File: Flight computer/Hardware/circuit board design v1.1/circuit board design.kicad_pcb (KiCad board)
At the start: 4 copper layers, 30.5 x 82.6 mm, 89 parts, among them J1 Conn_01x05, J2 USB_B_Micro, J3 Screw_Terminal_01x04, J4 Conn_01x02, J5 Screw_Terminal_01x04, J6 Conn_Coaxial, J7 Conn_Coaxial, U1 IIS2MDC, U10 BMI088, U11 W25Q64JVSSIM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

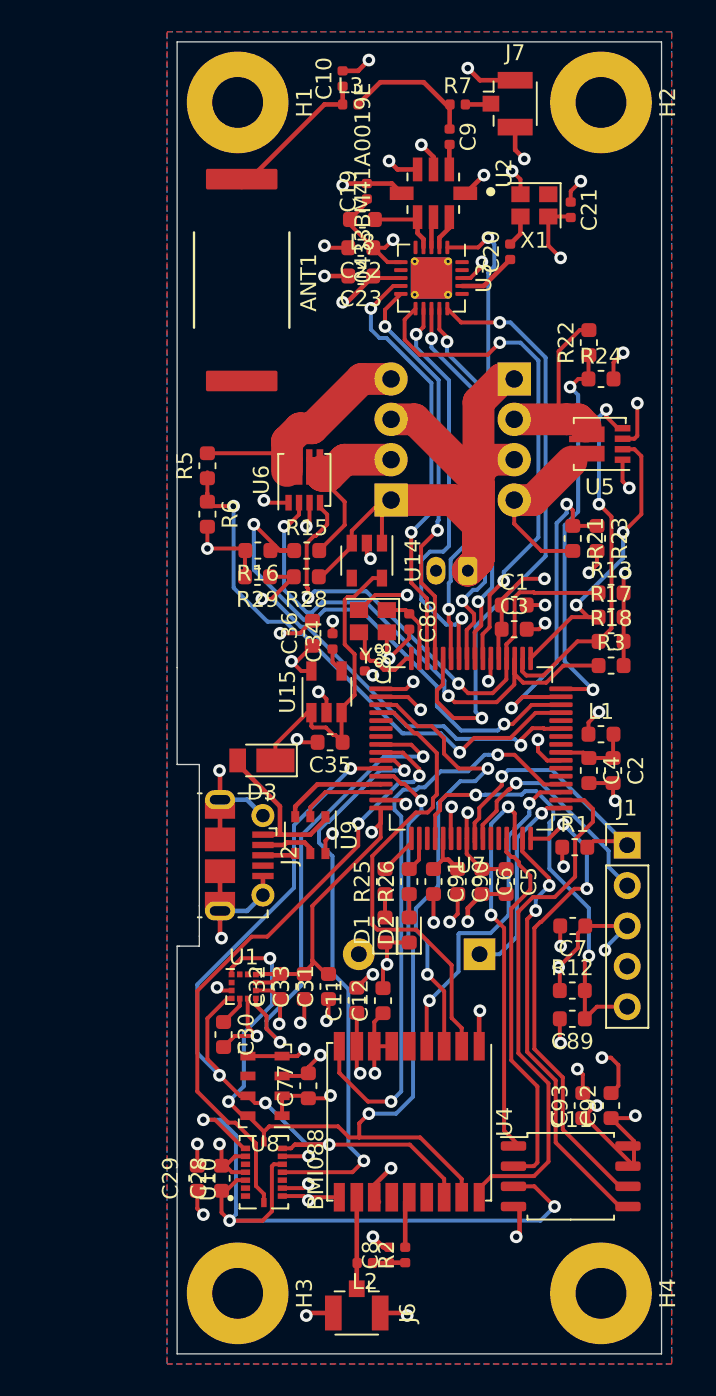
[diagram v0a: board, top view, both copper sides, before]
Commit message: wired up the news sensors
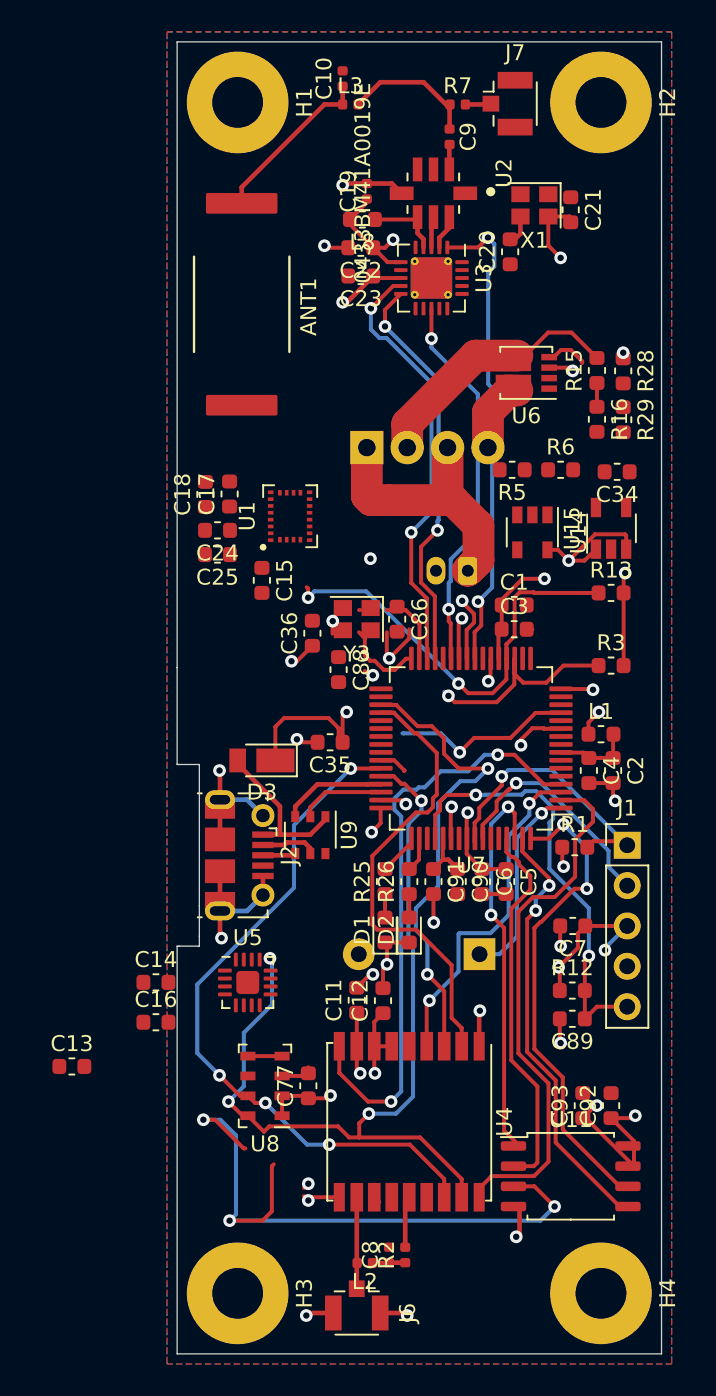
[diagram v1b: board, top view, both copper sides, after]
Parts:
- removed C28, C29, C31, C33: 100nF, Capacitor_SMD:C_0603_1608Metric
- removed C30: 220nF, Capacitor_SMD:C_0603_1608Metric
- removed C32: 10uF, Capacitor_SMD:C_0603_1608Metric
- removed J5: Screw_Terminal_01x04, flight-computer:TerminalBlock_TE_282834-4_1x04_P2.54mm_Horizontal
- removed R17, R18: 3.3K, Resistor_SMD:R_0603_1608Metric
- removed R21, R22: 100K, Resistor_SMD:R_0603_1608Metric
- removed R23, R24: 27K, Resistor_SMD:R_0603_1608Metric
- removed U10: BMI088, BMI088:PQFN50P450X300X100-16N
- added C13: 10uF, Capacitor_SMD:C_0603_1608Metric, F.Cu at (85.7, 122.3)
- added C14: 100nF, Capacitor_SMD:C_0603_1608Metric, F.Cu at (91.0, 117.0)
- added C15: 100nF, Capacitor_SMD:C_0603_1608Metric, F.Cu at (97.7, 91.7)
- added C16: 100nF, Capacitor_SMD:C_0603_1608Metric, F.Cu at (91.0, 119.5)
- added C17: 100nF, Capacitor_SMD:C_0603_1608Metric, F.Cu at (95.6, 86.2)
- added C18: 10uF, Capacitor_SMD:C_0603_1608Metric, F.Cu at (94.1, 86.3)
- added C24: 10nF, Capacitor_SMD:C_0603_1608Metric, F.Cu at (94.9, 88.5)
- added C25: 100nF, Capacitor_SMD:C_0603_1608Metric, F.Cu at (94.9, 90.0)
- C20, C21, C34, C86, C88: footprint Capacitor_SMD:C_0402_1005Metric -> Capacitor_SMD:C_0603_1608Metric
- U1: value IIS2MDC -> LSM9DS1; footprint Package_LGA:LGA-12_2x2mm_P0.5mm -> Package_LGA:LGA-24L_3x3.5mm_P0.43mm
- U15: value LD3985G33R_TSOT23 -> LD3985M33R_TSOT23
- U5: value Si7232DN -> H3LIS100DL; footprint Package_SO:Vishay_PowerPAK_1212-8_Dual -> Package_DFN_QFN:QFN-16-1EP_3x3mm_P0.5mm_EP1.45x1.45mm
- X1: footprint Crystal:Crystal_SMD_2520-4Pin_2.5x2.0mm -> flight-computer:Crystal_SMD_2520-4Pin_2.5x2.0mm
- moved U5 40.5 mm to (96.8, 117.0), turned to 0 degrees
- moved U1 29.7 mm to (99.4, 87.6), turned to 90 degrees
- moved R29 25.0 mm to (120.4, 81.6), turned to 270 degrees
- moved R28 23.8 mm to (120.4, 78.5), turned to 270 degrees
- moved R16 22.9 mm to (118.7, 81.5), turned to 270 degrees
- moved R6 22.4 mm to (116.5, 84.7), turned to 0 degrees
- moved R15 21.5 mm to (118.7, 78.5), turned to 90 degrees
- moved C34 20.8 mm to (120.0, 84.8), turned to 180 degrees
- moved U15 20.7 mm to (119.6, 88.4)
- moved R5 19.2 mm to (113.4, 84.7), turned to 180 degrees
- moved U6 15.5 mm to (114.3, 78.6), turned to 180 degrees
- moved U14 10.6 mm to (114.7, 88.6)
- moved J3 3.64 mm to (104.3, 83.3), turned to 0 degrees
- moved C88 1.70 mm to (102.5, 97.3)
- moved ANT1 1.52 mm to (96.4, 74.3)
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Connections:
- U1 pad 1: /gps/GPS_SCL -> +3V3
- U1 pad 10: +3V3 -> Net-(U1-Pad10)
- U1 pad 11: Net-(U1-Pad11) -> /sensors/ACCL_RDY
- U1 pad 12: Net-(U1-Pad12) -> /sensors/GYRO_RDY
- U1 pad 2: Net-(U1-Pad2) -> /gps/GPS_SCL
- U1 pad 5: Net-(C30-Pad1) -> +3V3
- U1 pad 6: GND -> +3V3
- U1 pad 7: /sensors/MAG_RDY -> +3V3
- U1 pad 8: GND -> +3V3
- U1 pad 9: +3V3 -> /sensors/MAG_RDY
- U5 pad 1: GND -> +3V3
- U5 pad 2: /pyro_driver/FIRE_C -> (no net)
- U5 pad 3: GND -> (no net)
- U5 pad 4: /pyro_driver/FIRE_D -> /gps/GPS_SCL
- U5 pad 5: /pyro_driver/FET_D -> GND
- U5 pad 6: /pyro_driver/FET_C -> /gps/GPS_SDA
- U7 pad 15: /MCU/MCU_PA06 -> Net-(U7-Pad15)
- U7 pad 16: /MCU/MCU_PA07 -> Net-(U7-Pad16)
- U7 pad 17: /pyro_driver/FIRE_C -> Net-(U7-Pad17)
- U7 pad 18: /pyro_driver/FIRE_D -> Net-(U7-Pad18)
- U7 pad 37: Net-(U7-Pad37) -> /sensors/GYRO_RDY
- U7 pad 38: Net-(U7-Pad38) -> /sensors/ACCL_RDY
- U7 pad 41: /sensors/ACCL_RDY -> /sensors/H_ACCL_INT1
- U7 pad 42: /sensors/GYRO_RDY -> /sensors/H_ACCL_INT2
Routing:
- net GND: track 158.6 -> 72.4 mm, vias 64 -> 25
- net +3V3: track 278.7 -> 222.4 mm, vias 23 -> 20
- net /sensors/ACCL_RDY: track 39.0 -> 0.00 mm, vias 2 -> 0
- net /MCU/MCU_NSEL1: track 38.2 -> 0.00 mm, vias 2 -> 0
- net /sensors/GYRO_RDY: track 36.1 -> 0.00 mm, vias 2 -> 0
- net Vdrive: track 53.2 -> 19.4 mm, vias 0 -> 1
- net /MCU/MCU_PB10: track 32.0 -> 0.00 mm, vias 2 -> 0
- net /MCU/MCU_PA05: track 33.0 -> 2.39 mm, vias 2 -> 0
- net /sensors/MAG_RDY: track 30.4 -> 0.00 mm, vias 2 -> 0
- net /MCU/MCU_PA07: track 25.3 -> 0.00 mm, vias 2 -> 0
- net /MCU/MCU_PB08: track 27.4 -> 3.16 mm, vias 2 -> 1
- net /MCU/MCU_SCLK1: track 26.6 -> 2.63 mm, vias 2 -> 1
- net /pyro_driver/FIRE_D: track 23.8 -> 0.00 mm, vias 2 -> 0
- net /MCU/MCU_PA04: track 34.8 -> 11.5 mm, vias 2 -> 1
- net /MCU/MCU_PA06: track 20.7 -> 0.00 mm, vias 2 -> 0
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
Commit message: Fully routed board v1.1 with the new high g accelerometer
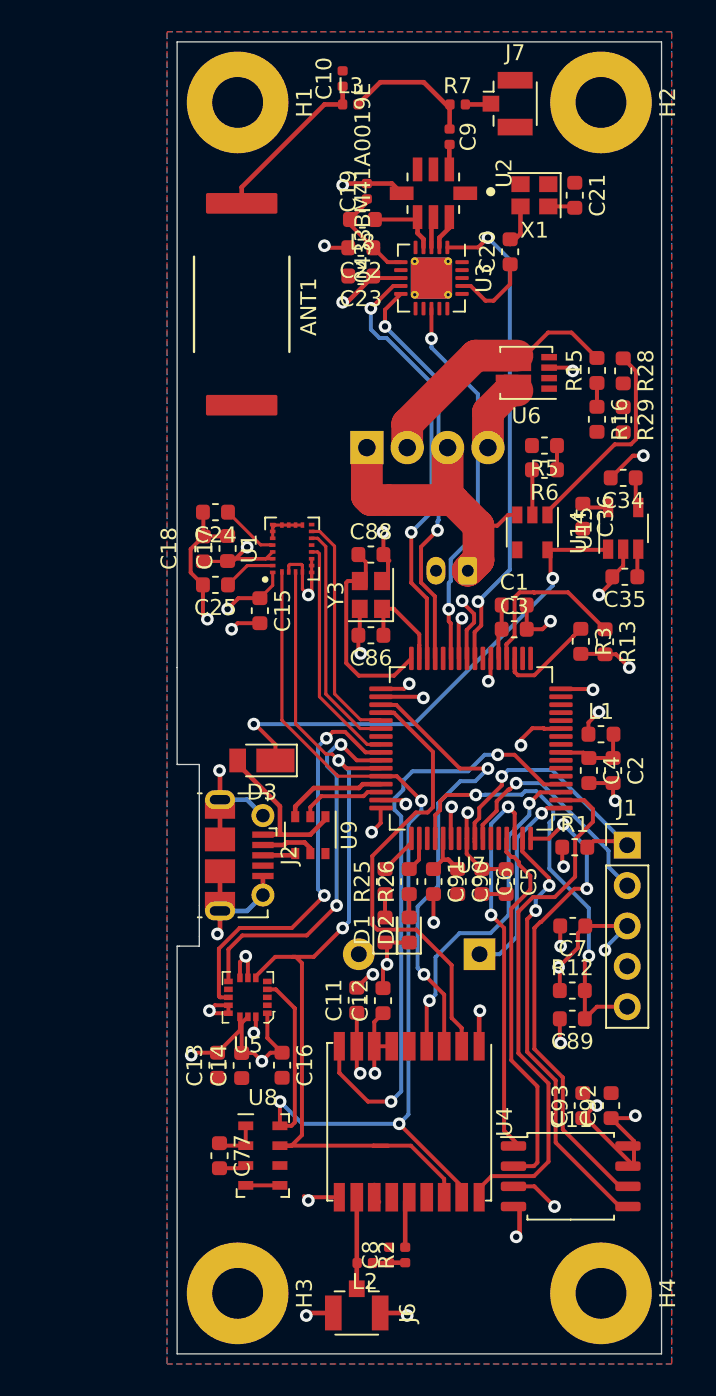
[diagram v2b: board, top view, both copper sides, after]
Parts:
- U5: footprint Package_DFN_QFN:QFN-16-1EP_3x3mm_P0.5mm_EP1.45x1.45mm -> flight-computer:TFLGA-16_3x3mm
- moved C35 21.3 mm to (120.5, 91.4)
- moved C36 18.5 mm to (117.9, 87.6), turned to 270 degrees
- moved C13 9.16 mm to (94.9, 122.2), turned to 90 degrees
- moved C16 8.38 mm to (98.9, 122.2), turned to 270 degrees
- moved C88 7.52 mm to (104.5, 90.0), turned to 0 degrees
- moved C14 7.52 mm to (96.4, 122.2), turned to 90 degrees
- moved C77 7.11 mm to (95.0, 127.9), turned to 270 degrees
- moved U8 4.39 mm to (97.7, 127.9), turned to 0 degrees
- moved C17 3.43 mm to (95.5, 89.7)
- moved C18 3.43 mm to (94.0, 89.7)
- moved R13 3.10 mm to (119.3, 95.5), turned to 270 degrees
- moved R5 2.54 mm to (115.4, 83.2)
- moved R3 2.44 mm to (117.7, 95.5), turned to 270 degrees
- moved U1 2.04 mm to (99.6, 89.7)
- moved C86 1.94 mm to (104.5, 95.1), turned to 180 degrees
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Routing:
- net +3V3: track 222.4 -> 171.5 mm, vias 20 -> 19
- net GND: track 72.4 -> 100.5 mm, vias 25 -> 30
- net /sensors/H_ACCL_INT1: track 0.00 -> 26.0 mm, vias 0 -> 2
- net /sensors/H_ACCL_INT2: track 1.77 -> 23.8 mm, vias 0 -> 2
- net /pyro_driver/FIRE_B: track 29.8 -> 10.9 mm, vias 2 -> 0
- net /gps/GPS_SDA: track 43.8 -> 60.4 mm, vias 4 -> 2
- net Vdrive: track 19.4 -> 35.2 mm, vias 1 -> 0
- net /sensors/ACCL_RDY: track 0.00 -> 14.8 mm
- net /sensors/GYRO_RDY: track 0.00 -> 14.7 mm
- net /sensors/MAG_RDY: track 0.00 -> 14.6 mm
- net /gps/GPS_SCL: track 56.0 -> 67.8 mm, vias 4 -> 3
- net /MCU/MCU_PA04: track 11.5 -> 1.52 mm, vias 1 -> 0
- net /pyro_driver/FIRE_A: track 13.7 -> 6.31 mm, vias 1 -> 0
- net /MCU/XOUT: track 5.19 -> 12.5 mm
- net Net-(C35-Pad1): track 39.8 -> 33.7 mm
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
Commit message: flood fill top and bottom layers
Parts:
- moved C15 2.68 mm to (97.3, 96.2)
- moved C18 2.68 mm to (93.7, 92.4)
- moved C24 2.68 mm to (94.5, 90.0)
- moved C25 2.68 mm to (94.5, 94.6)
- moved C17 2.68 mm to (95.2, 92.3)
- moved U1 2.68 mm to (99.3, 92.3)
- moved R13 1.66 mm to (117.6, 95.4)
- moved J4 1.52 mm to (110.6, 89.5)
- moved R3 1.40 mm to (119.1, 95.4)
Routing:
- net GND: track 100.5 -> 172.5 mm, vias 30 -> 53
- net /MCU/MCU_NSEL1: track 0.00 -> 37.6 mm, vias 0 -> 2
- net /MCU/MCU_PB10: track 0.00 -> 32.2 mm, vias 0 -> 2
- net /MCU/MCU_PB08: track 3.16 -> 30.9 mm, vias 1 -> 2
- net /MCU/MCU_SCLK1: track 2.63 -> 27.6 mm, vias 1 -> 2
- net /MCU/MCU_MOSI1: track 4.15 -> 28.4 mm, vias 1 -> 2
- net /MCU/MCU_PA04: track 1.52 -> 24.2 mm, vias 0 -> 2
- net /MCU/MCU_PA05: track 2.39 -> 24.9 mm, vias 0 -> 2
- net /pyro_driver/FIRE_A: track 6.31 -> 28.7 mm, vias 0 -> 2
- net /pyro_driver/FIRE_B: track 10.9 -> 29.5 mm, vias 0 -> 2
- net +3V3: track 171.5 -> 180.3 mm, vias 19 -> 25
- net /MCU/MCU_MISO1: track 24.0 -> 32.2 mm
- net /MCU/MCU_PA12: track 25.6 -> 33.6 mm, vias 2 -> 0
- net /MCU/MCU_PA13: track 27.3 -> 34.4 mm, vias 2 -> 0
- net /pyro_driver/FET_A: track 4.65 -> 9.31 mm
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- added copper zone on B.Cu, net (none)
- removed copper zone on B.Cu, net GND

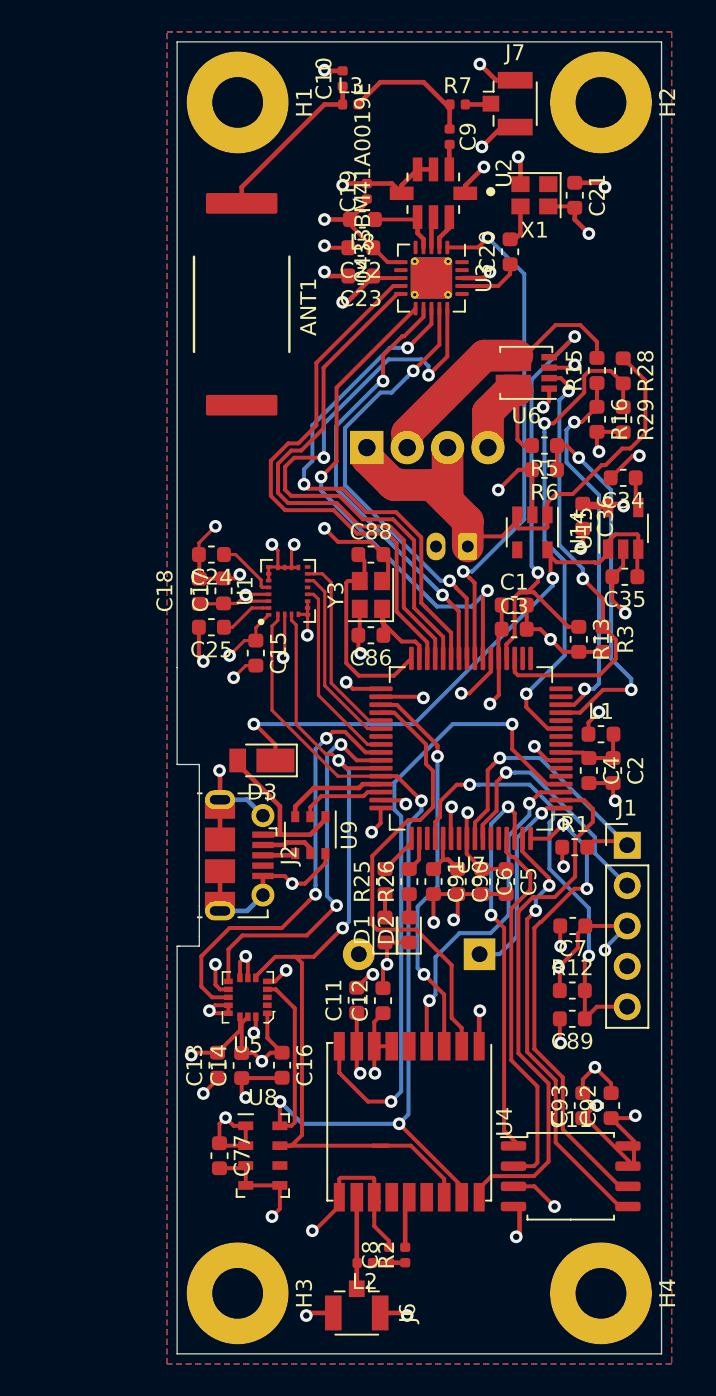
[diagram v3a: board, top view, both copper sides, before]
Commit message: put in logo for V1.1
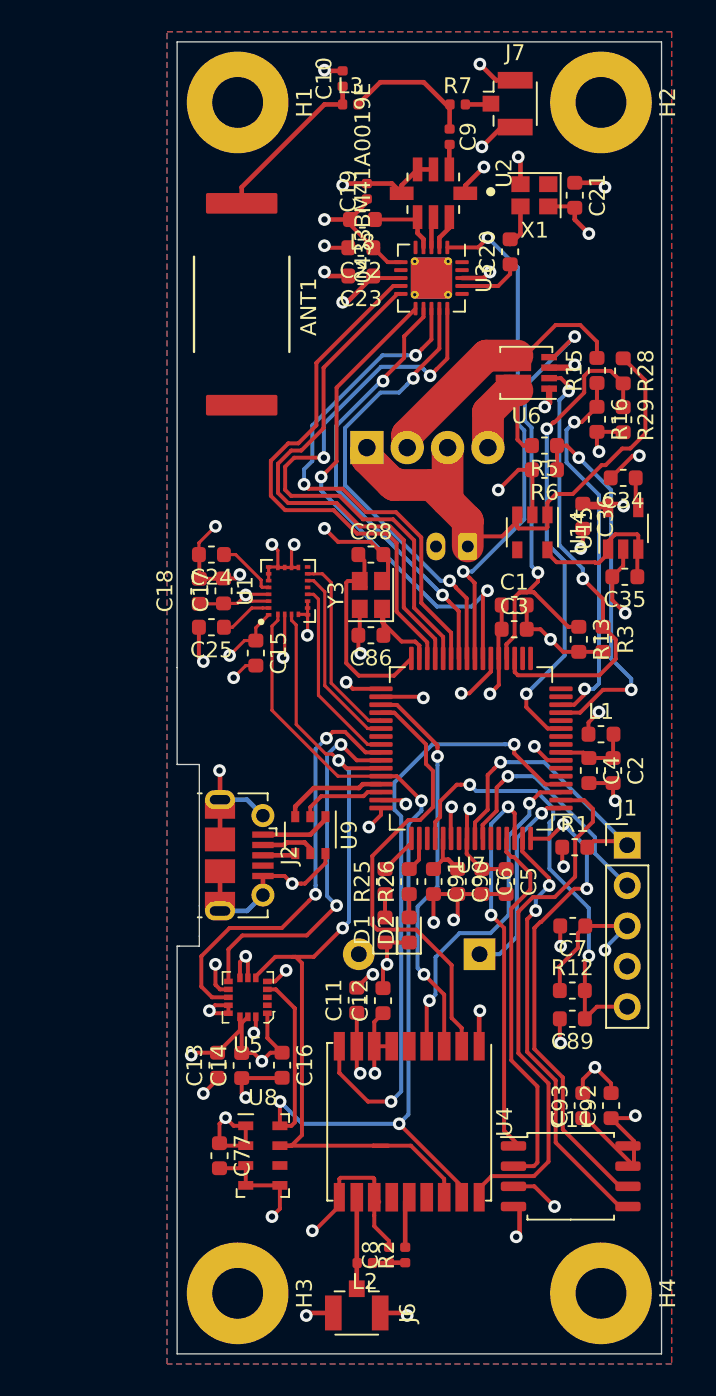
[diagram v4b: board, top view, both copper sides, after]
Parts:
- removed D3: DFLS130L, Diode_SMD:D_PowerDI-123
- added G***: LOGO, flight-computer:ICSS_Logo, B.Cu at (107.4, 99.8)
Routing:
- net +3V3: track 180.3 -> 109.5 mm, vias 25 -> 23
- net Net-(C35-Pad1): track 38.2 -> 10.0 mm, vias 2 -> 0
- net VBUS: track 11.8 -> 4.98 mm
- net /gps/GPS_NRES: track 40.7 -> 39.0 mm
- net /MCU/MCU_NSEL1: track 37.6 -> 36.9 mm
- net /MCU/MCU_MISO1: track 32.2 -> 32.8 mm

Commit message: connected flood fill of bottom layer to gnd
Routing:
- added copper zone on B.Cu, net GND
- removed copper zone on B.Cu, net (none)
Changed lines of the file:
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@@
     )
   )
-  (zone (net 0) (net_name "") (layer B.Cu) (hatch edge 0.508)
+  (zone (net 1) (net_name GND) (layer B.Cu) (hatch edge 0.508)
     (connect_pads (clearance 0.508))
     (min_thickness 0.254)
